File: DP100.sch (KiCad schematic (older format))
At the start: 60 parts, among them J1 SMA CONNECTOR, J2 Conn_01x06, J3 Conn_02x06_Odd_Even, Q1 2N7002, U1 NCP1117-3.3_SOT223, U2 Si5351A-B-GT, U3 AD9215BRUZ, Y1 25MHZ

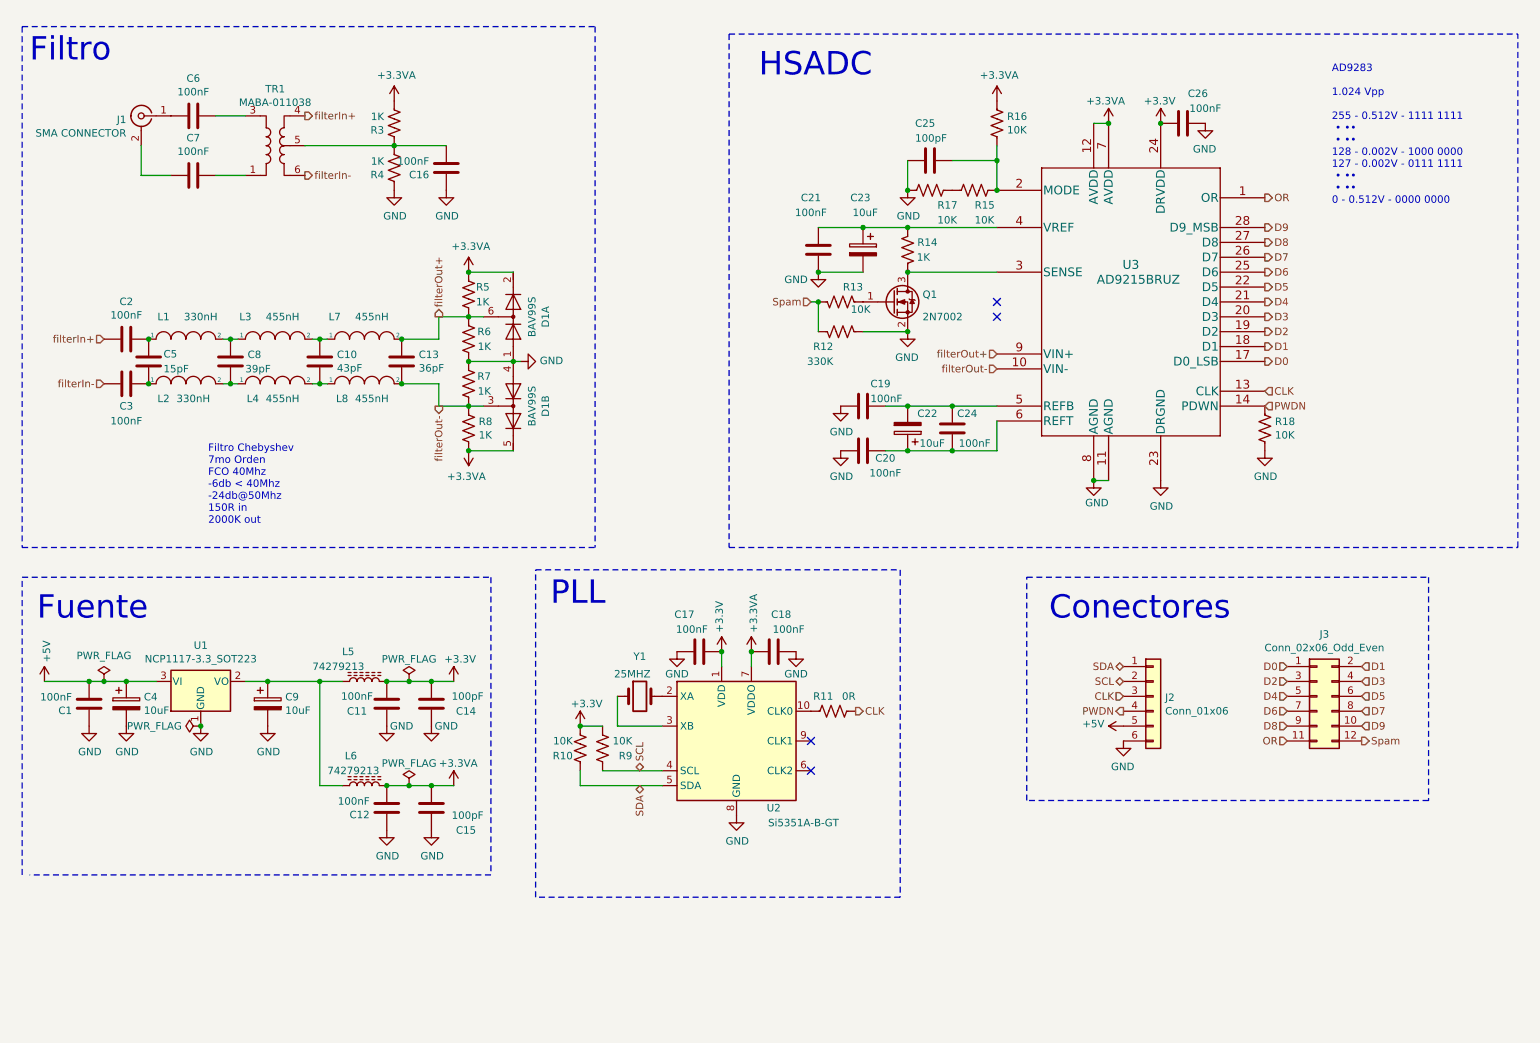
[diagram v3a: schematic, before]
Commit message: Se cambian las etiquetas jerarquicas por net labels.
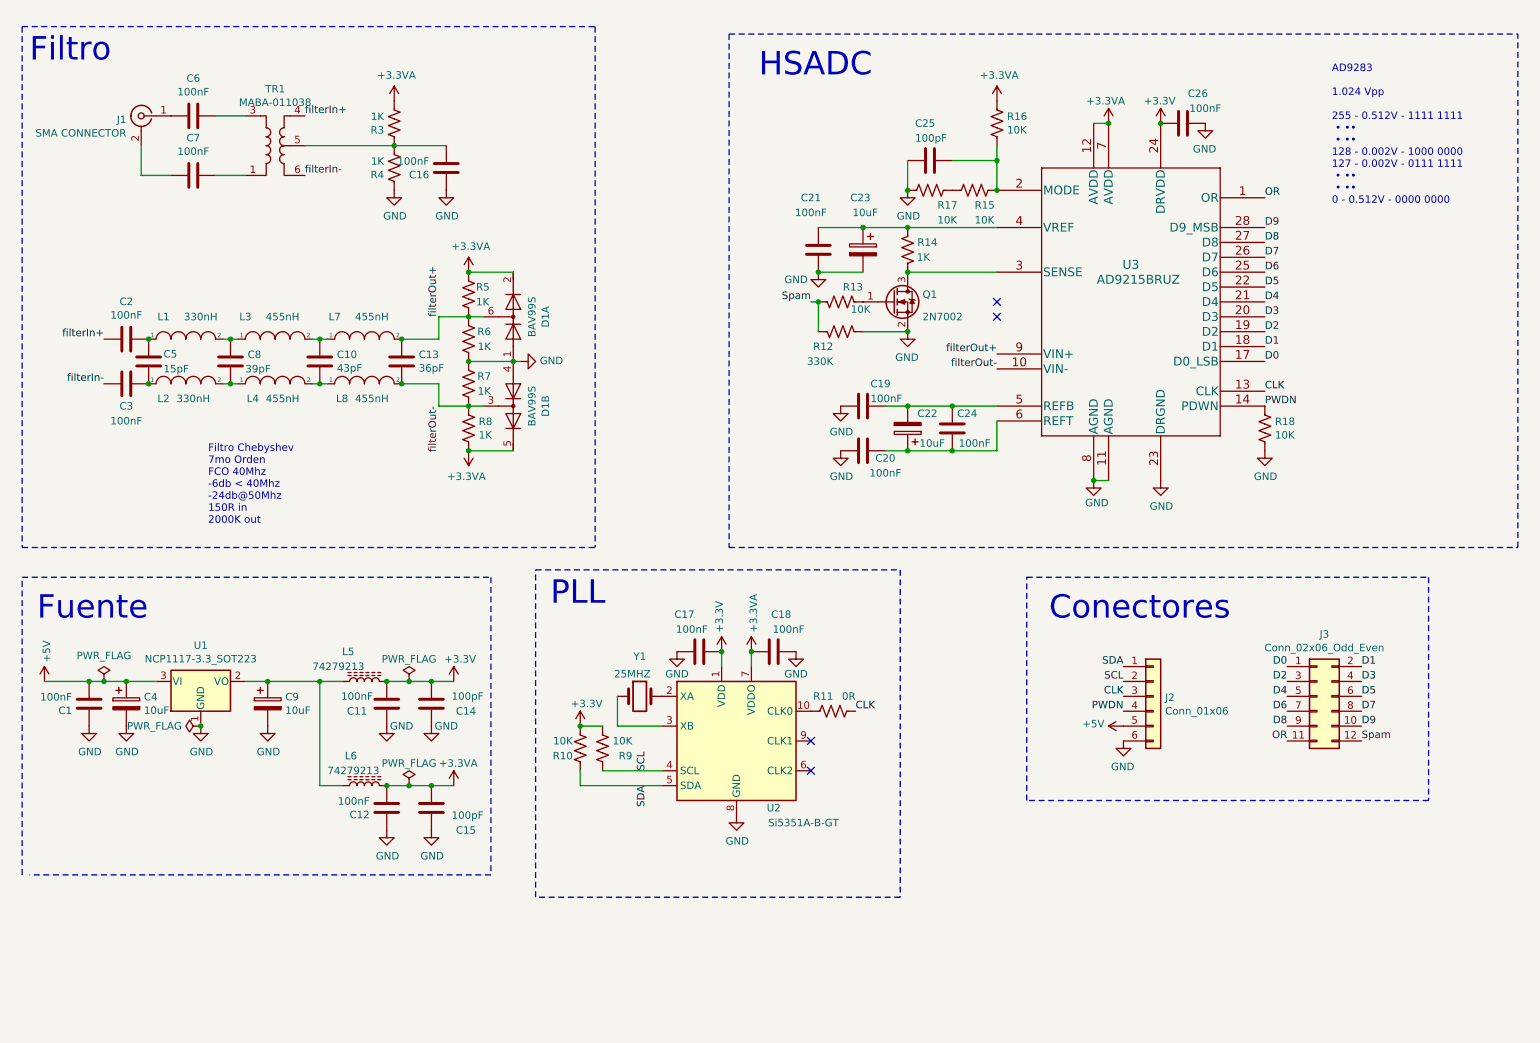
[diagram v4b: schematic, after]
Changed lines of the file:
@@
 Wire Notes Line
 	850  850  850  4350
-Text HLabel 1400 2950 0    50   Input ~ 0
-filterIn+
-Text HLabel 1400 3250 0    50   Input ~ 0
-filterIn-
-Text HLabel 2750 1450 2    50   Output ~ 0
-filterIn+
-Text HLabel 2750 1850 2    50   Output ~ 0
-filterIn-
-Text HLabel 3650 2800 1    50   Output ~ 0
-filterOut+
-Text HLabel 3650 3400 3    50   Output ~ 0
-filterOut-
-Text HLabel 7400 3050 0    50   Input ~ 0
-filterOut+
-Text HLabel 7400 3150 0    50   Input ~ 0
-filterOut-
-Text HLabel 5000 5850 1    50   BiDi ~ 0
-SCL
-Text HLabel 8250 5250 0    50   BiDi ~ 0
-SCL
-Text HLabel 5000 5950 3    50   BiDi ~ 0
-SDA
-Text HLabel 8250 5150 0    50   BiDi ~ 0
-SDA
-Text HLabel 6450 5450 2    50   Output ~ 0
-CLK
-Text HLabel 8250 5350 0    50   Input ~ 0
-CLK
-Text HLabel 8250 5450 0    50   Output ~ 0
-PWDN
-Text HLabel 9850 5650 2    50   Output ~ 0
-Spam
-Text HLabel 9850 5150 2    50   Input ~ 0
-D1
-Text HLabel 9850 5250 2    50   Input ~ 0
-D3
-Text HLabel 9850 5350 2    50   Input ~ 0
-D5
-Text HLabel 9850 5450 2    50   Input ~ 0
-D7
-Text HLabel 9850 5550 2    50   Input ~ 0
-D9
-Text HLabel 9350 5650 0    50   Input ~ 0
-OR
-Text HLabel 9350 5550 0    50   Input ~ 0
-D8
-Text HLabel 9350 5450 0    50   Input ~ 0
-D6
-Text HLabel 9350 5350 0    50   Input ~ 0
-D4
-Text HLabel 9350 5250 0    50   Input ~ 0
-D2
-Text HLabel 9350 5150 0    50   Input ~ 0
-D0
-Text HLabel 9200 3300 2    50   Input ~ 0
-CLK
-Text HLabel 9200 3400 2    50   Input ~ 0
-PWDN
 Wire Wire Line
 	2750 1650 3350 1650
-Text HLabel 6150 2700 0    50   Input ~ 0
-Spam
-Text HLabel 9200 2200 2    50   Output ~ 0
-D9
-Text HLabel 9200 2000 2    50   Output ~ 0
-OR
-Text HLabel 9200 2300 2    50   Output ~ 0
-D8
-Text HLabel 9200 2400 2    50   Output ~ 0
-D7
-Text HLabel 9200 2500 2    50   Output ~ 0
-D6
-Text HLabel 9200 2600 2    50   Output ~ 0
-D5
-Text HLabel 9200 2700 2    50   Output ~ 0
-D4
-Text HLabel 9200 2800 2    50   Output ~ 0
-D3
-Text HLabel 9200 2900 2    50   Output ~ 0
-D2
-Text HLabel 9200 3000 2    50   Output ~ 0
-D1
-Text HLabel 9200 3100 2    50   Output ~ 0
-D0
 Connection ~ 7400 1950
 $Comp
@@
 	1    0    0    -1
 $EndComp
+Text Label 1400 2950 2    50   ~ 0
+filterIn+
+Text Label 1400 3250 2    50   ~ 0
+filterIn-
+Text Label 7400 3050 2    50   ~ 0
+filterOut+
+Text Label 7400 3150 2    50   ~ 0
+filterOut-
+Text Label 2750 1450 0    50   ~ 0
+filterIn+
+Text Label 2750 1850 0    50   ~ 0
+filterIn-
+Text Label 3650 2800 1    50   ~ 0
+filterOut+
+Text Label 3650 3400 3    50   ~ 0
+filterOut-
+Text Label 9200 3300 0    50   ~ 0
+CLK
+Text Label 8250 5250 2    50   ~ 0
+SCL
+Text Label 8250 5150 2    50   ~ 0
+SDA
+Text Label 6450 5450 0    50   ~ 0
+CLK
+Text Label 5050 5850 1    50   ~ 0
+SCL
+Text Label 5050 5950 3    50   ~ 0
+SDA
+Text Label 8250 5350 2    50   ~ 0
+CLK
+Text Label 9200 3400 0    50   ~ 0
+PWDN
+Text Label 8250 5450 2    50   ~ 0
+PWDN
+Text Label 6150 2700 2    50   ~ 0
+Spam
+Text Label 9850 5650 0    50   ~ 0
+Spam
+Text Label 9200 2000 0    50   ~ 0
+OR
+Text Label 9200 2200 0    50   ~ 0
+D9
+Text Label 9200 2300 0    50   ~ 0
+D8
+Text Label 9200 2400 0    50   ~ 0
+D7
+Text Label 9200 2500 0    50   ~ 0
+D6
+Text Label 9200 2600 0    50   ~ 0
+D5
+Text Label 9200 2700 0    50   ~ 0
+D4
+Text Label 9200 2800 0    50   ~ 0
+D3
+Text Label 9200 2900 0    50   ~ 0
+D2
+Text Label 9200 3000 0    50   ~ 0
+D1
+Text Label 9200 3100 0    50   ~ 0
+D0
+Text Label 9350 5650 2    50   ~ 0
+OR
+Text Label 9850 5550 0    50   ~ 0
+D9
+Text Label 9350 5550 2    50   ~ 0
+D8
+Text Label 9850 5450 0    50   ~ 0
+D7
+Text Label 9350 5450 2    50   ~ 0
+D6
+Text Label 9850 5350 0    50   ~ 0
+D5
+Text Label 9350 5350 2    50   ~ 0
+D4
+Text Label 9850 5250 0    50   ~ 0
+D3
+Text Label 9850 5150 0    50   ~ 0
+D1
+Text Label 9350 5150 2    50   ~ 0
+D0
+Text Label 9350 5250 2    50   ~ 0
+D2
 $EndSCHEMATC

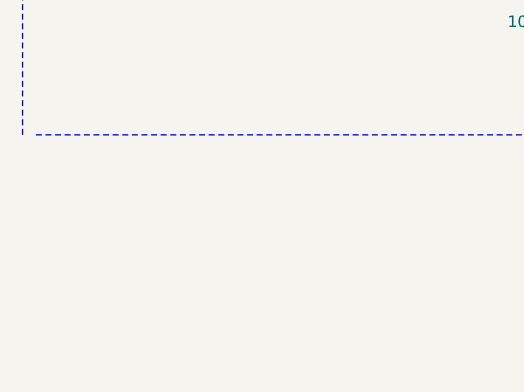
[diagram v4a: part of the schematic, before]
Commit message: Se agregan correcciones realizadas por Francisco Timez el dia 10-4 -Fiduciarios -Serigrafias faltantes -Otro agujero de sujecion
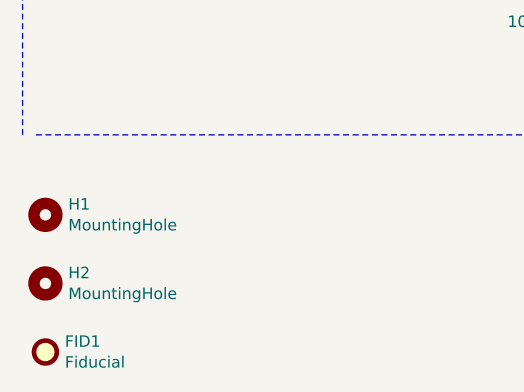
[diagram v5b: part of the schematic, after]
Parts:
- added FID1: Fiducial, Fiducial:Fiducial_0.5mm_Mask1mm, symbol Mechanical:Fiducial
- added H1, H2: MountingHole, MountingHole:MountingHole_3mm, symbol Mechanical:MountingHole
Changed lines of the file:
@@
 Text Label 9350 5250 2    50   ~ 0
 D2
+$Comp
+L Mechanical:MountingHole H1
+U 1 1 607472D1
+P 950 6900
+F 0 "H1" H 1050 6946 50  0000 L CNN
+F 1 "MountingHole" H 1050 6855 50  0000 L CNN
+F 2 "MountingHole:MountingHole_3mm" H 950 6900 50  0001 C CNN
+F 3 "~" H 950 6900 50  0001 C CNN
+	1    950  6900
+	1    0    0    -1
+$EndComp
+$Comp
+L Mechanical:MountingHole H2
+U 1 1 6074792D
+P 950 7200
+F 0 "H2" H 1050 7246 50  0000 L CNN
+F 1 "MountingHole" H 1050 7155 50  0000 L CNN
+F 2 "MountingHole:MountingHole_3mm" H 950 7200 50  0001 C CNN
+F 3 "~" H 950 7200 50  0001 C CNN
+	1    950  7200
+	1    0    0    -1
+$EndComp
+$Comp
+L Mechanical:Fiducial FID1
+U 1 1 60757A68
+P 950 7500
+F 0 "FID1" H 1035 7546 50  0000 L CNN
+F 1 "Fiducial" H 1035 7455 50  0000 L CNN
+F 2 "Fiducial:Fiducial_0.5mm_Mask1mm" H 950 7500 50  0001 C CNN
+F 3 "~" H 950 7500 50  0001 C CNN
+	1    950  7500
+	1    0    0    -1
+$EndComp
 $EndSCHEMATC

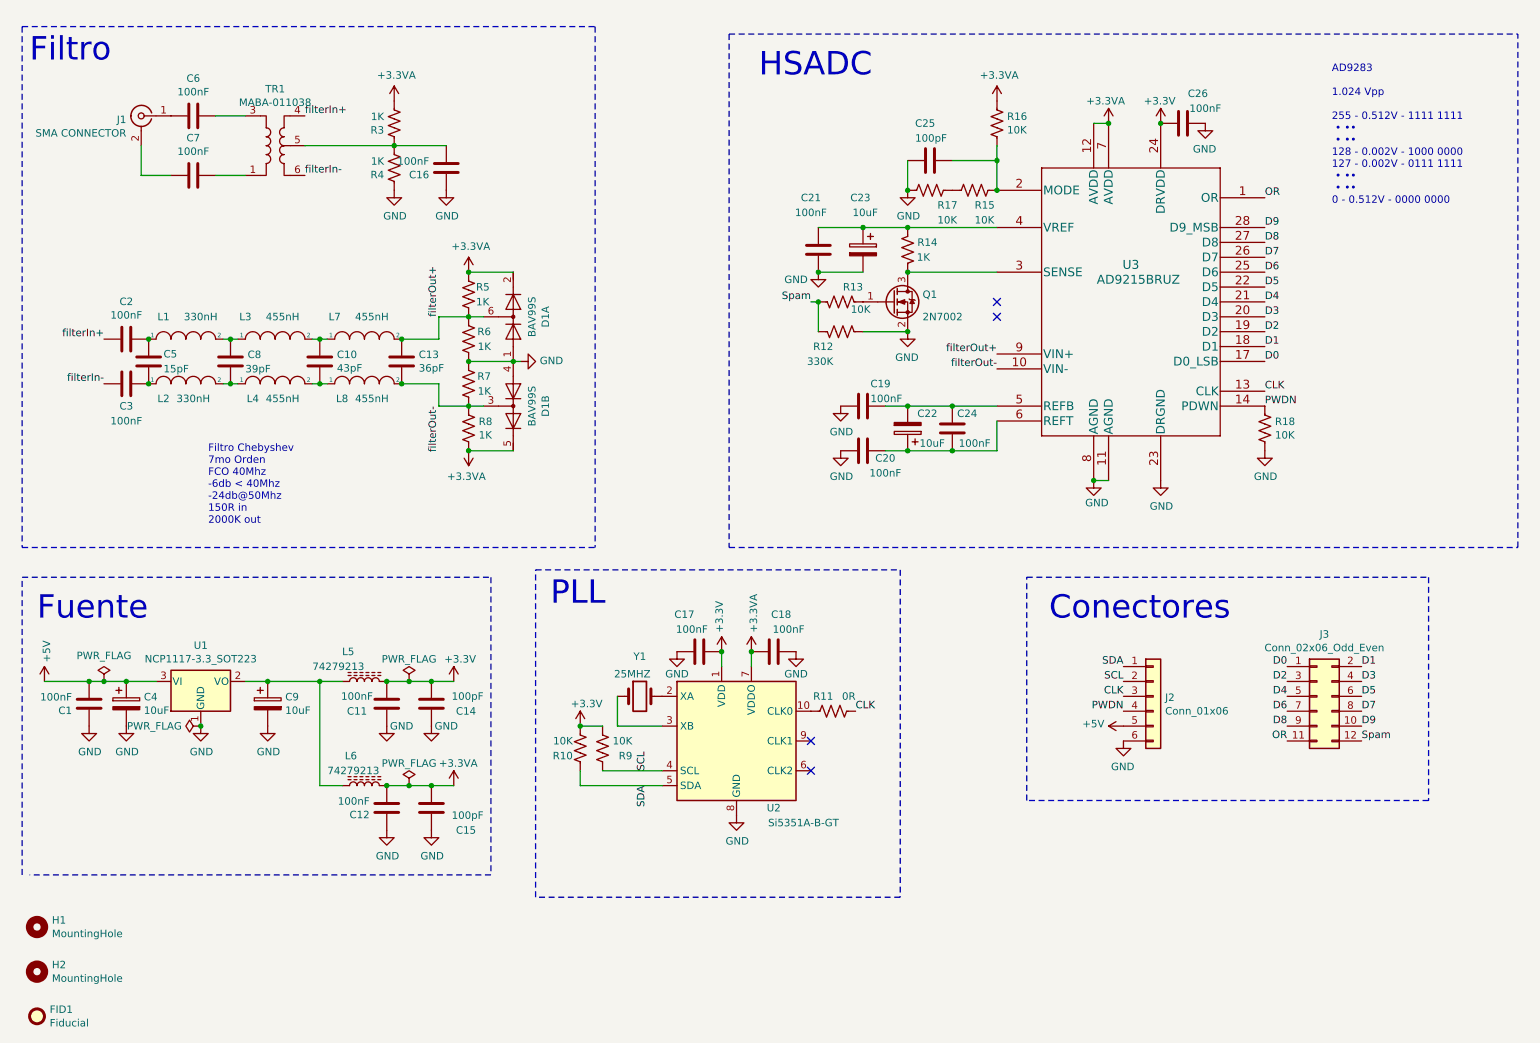
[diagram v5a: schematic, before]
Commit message: Correcciones en base a devolucion de Diego Brengi del dia 12-4-2021 -Se expanden las zonas compactas -Se agrega directorio con informacion extra -Se agregan lineas para evitar que los labels toquen directamente el componente -Se agrega bus para unir los pines Dn -Se agrega referencia  a la licencia -Se remueven las etiquetas filterIn
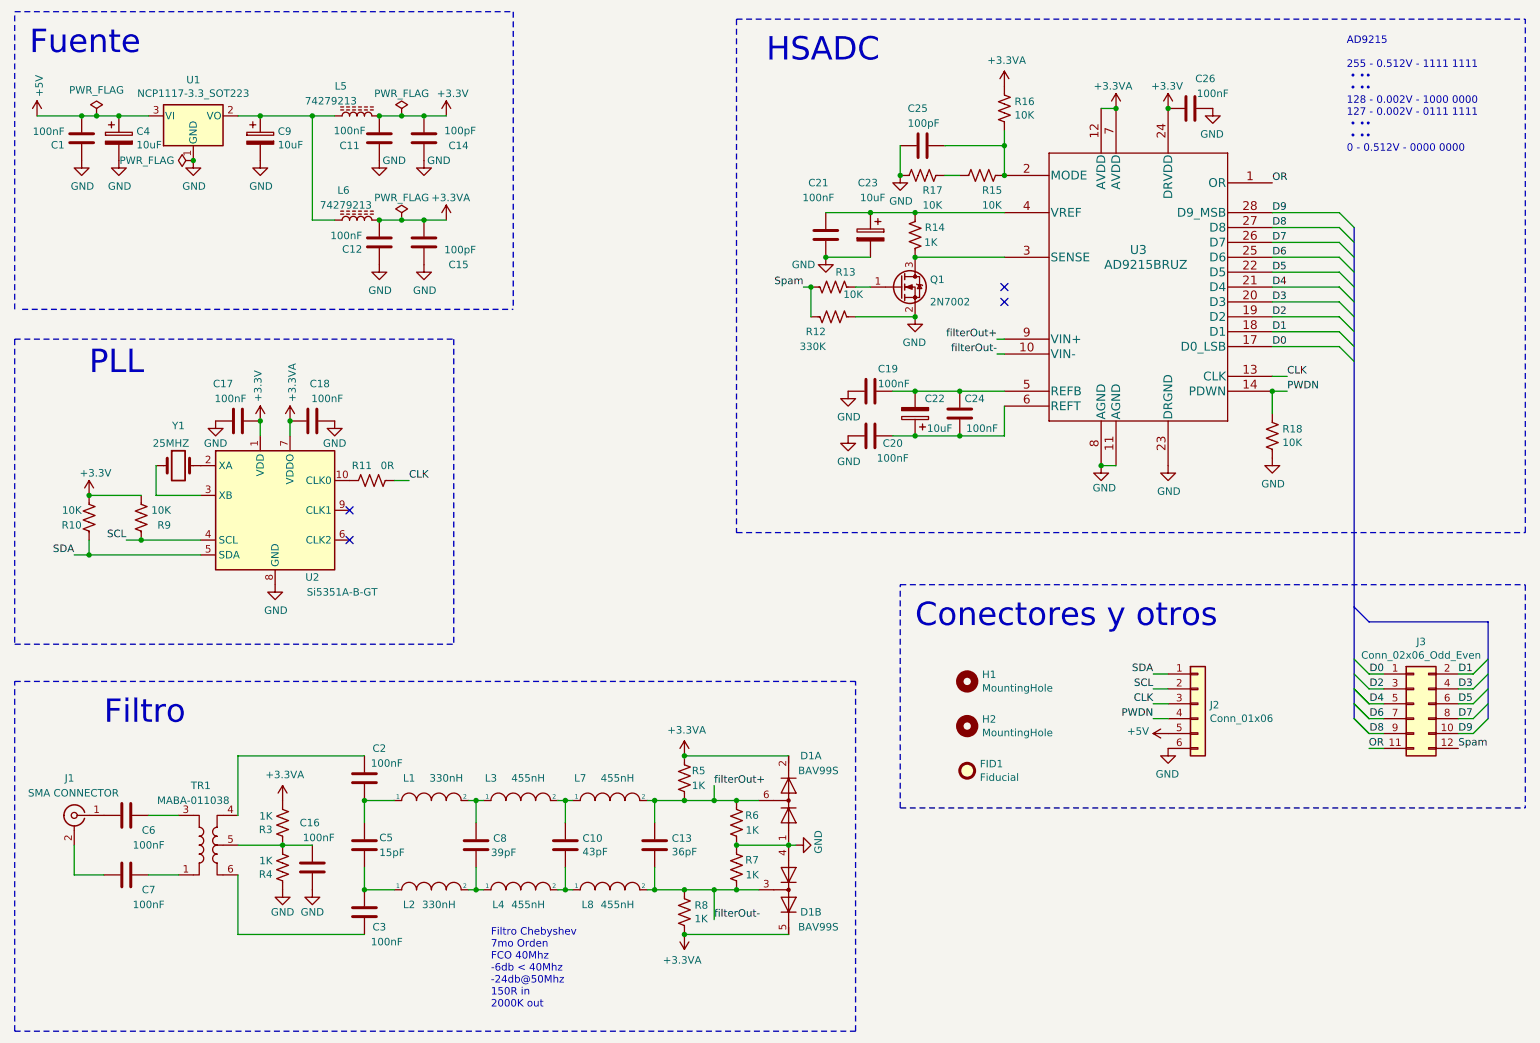
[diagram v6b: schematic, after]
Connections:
- net filterIn+: no longer names the net of C2.2, TR1.4
- net filterIn-: no longer names the net of C3.2, TR1.6
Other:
- note added: "AD9215\n\n255 - 0.512V - 1111 1111\n • ••\n • ••\n128 - 0.002V - 1000 0000\n127 - 0.002V - 0111 1111\n • ••\n • ••\n0 - 0.512V - 0000 0000"
- note added: "Conectores y otros"
- note removed: "AD9283\n\n1.024 Vpp\n\n255 - 0.512V - 1111 1111\n • ••\n • ••\n128 - 0.002V - 1000 0000\n127 - 0.002V - 0111 1111\n • ••\n • ••\n0 - 0.512V - 0000 0000"
- note removed: "Conectores"
- moved on the sheet: C1, C10, C11, C12, C13, C14, C15, C16, C17, C18, C19, C2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
